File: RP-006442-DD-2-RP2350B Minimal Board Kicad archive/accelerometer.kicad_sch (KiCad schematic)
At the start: 4 parts, among them U12 LIS2DW12TR

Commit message: Revert "Merge branch 'main' of https://github.com/alvestav/alvestav-lee-thesis-project-2025"
This reverts commit 492c910224f218c530b72a86f026f374fdb1ba99, reversing
changes made to 8b8c3067a07da89d4cec6960bc27222e60866367.
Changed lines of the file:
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@@
+		(color 0 0 0 0)
+	)
+	(junction
+		(at 171.45 110.49)
+		(diameter 0)
 		(color 0 0 0 0)
 	)
@@
 		(pts
 			(xy 195.58 101.6) (xy 207.01 101.6)
+		)
+		(stroke
+			(width 0)
+			(type default)
+		)
+	)
+	(wire
+		(pts
+			(xy 171.45 110.49) (xy 171.45 114.3)
 		)
 		(stroke
@@
 	(wire
 		(pts
+			(xy 165.1 110.49) (xy 171.45 110.49)
+		)
+		(stroke
+			(width 0)
+			(type default)
+		)
+	)
+	(wire
+		(pts
 			(xy 114.3 101.6) (xy 114.3 81.28)
 		)
@@
 	(wire
 		(pts
-			(xy 171.45 106.68) (xy 171.45 114.3)
+			(xy 171.45 106.68) (xy 171.45 110.49)
 		)
 		(stroke

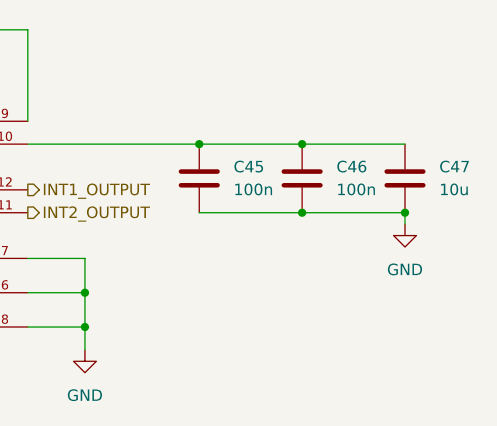
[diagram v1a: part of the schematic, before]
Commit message: Added LCSC numbers to parts
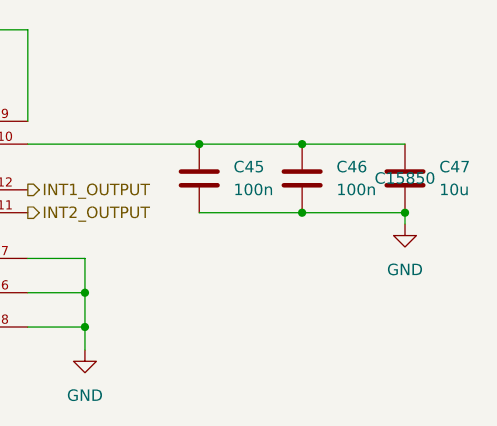
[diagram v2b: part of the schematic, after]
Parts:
- C47: LCSC (none) -> C15850
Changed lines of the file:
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@@
+			)
+		)
+		(property "LCSC" "C15850"
+			(at 207.01 97.79 0)
+			(effects
+				(font
+					(size 1.27 1.27)
+				)
 			)
 		)
